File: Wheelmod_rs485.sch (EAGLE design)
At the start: 52 parts, among them IC1 SN75176BPSR, SW1 RST_SW, SW2 HWB_SW, U1 ATMEGA8U2AU, U2 SI8441IS1, U3 MC33887-HSOP, U4 NFET-SOIC8, U5 LDO, X1 MINI-USB, X2 MICROMATCH-4, X3 ENC, X4 MICROMATCH-4, X5 LOGIC_IN, Y1 SMDRESONATOR

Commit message: Testing
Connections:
- net A: no longer R5.1
- net B: no longer R5.2
- net RX: now also R5.2
- net TX: now also R5.1
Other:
- moved on the sheet: IC1, R5
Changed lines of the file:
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@@
 <?xml version="1.0" encoding="utf-8"?>
 <!DOCTYPE eagle SYSTEM "eagle.dtd">
-<eagle version="6.5.0">
+<eagle version="7.1.0">
 <drawing>
 <settings>
@@
 <instance part="C14" gate="G$1" x="170.18" y="119.38"/>
 <instance part="GND23" gate="1" x="170.18" y="109.22"/>
-<instance part="IC1" gate="G$1" x="-53.34" y="119.38"/>
-<instance part="R5" gate="G$1" x="-27.94" y="119.38" rot="R90"/>
-<instance part="P+5" gate="VCC" x="-38.1" y="134.62"/>
-<instance part="GND16" gate="1" x="-38.1" y="106.68"/>
+<instance part="IC1" gate="G$1" x="-38.1" y="121.92"/>
+<instance part="R5" gate="G$1" x="-66.04" y="121.92" rot="R90"/>
+<instance part="P+5" gate="VCC" x="-22.86" y="137.16"/>
+<instance part="GND16" gate="1" x="-22.86" y="109.22"/>
 <instance part="X2" gate="-1" x="-2.54" y="127"/>
 <instance part="X2" gate="-2" x="-2.54" y="124.46"/>
@@
 <pinref part="IC1" gate="G$1" pin="GND"/>
 <pinref part="GND16" gate="1" pin="GND"/>
-<wire x1="-40.64" y1="111.76" x2="-38.1" y2="111.76" width="0.1524" layer="91"/>
-<wire x1="-38.1" y1="111.76" x2="-38.1" y2="109.22" width="0.1524" layer="91"/>
+<wire x1="-25.4" y1="114.3" x2="-22.86" y2="114.3" width="0.1524" layer="91"/>
+<wire x1="-22.86" y1="114.3" x2="-22.86" y2="111.76" width="0.1524" layer="91"/>
 </segment>
 <segment>
@@
 <pinref part="IC1" gate="G$1" pin="VCC"/>
 <pinref part="P+5" gate="VCC" pin="VCC"/>
-<wire x1="-40.64" y1="127" x2="-38.1" y2="127" width="0.1524" layer="91"/>
-<wire x1="-38.1" y1="127" x2="-38.1" y2="132.08" width="0.1524" layer="91"/>
+<wire x1="-25.4" y1="129.54" x2="-22.86" y2="129.54" width="0.1524" layer="91"/>
+<wire x1="-22.86" y1="129.54" x2="-22.86" y2="134.62" width="0.1524" layer="91"/>
 </segment>
 <segment>
@@
 <segment>
 <pinref part="IC1" gate="G$1" pin="R"/>
-<wire x1="-66.04" y1="127" x2="-73.66" y2="127" width="0.1524" layer="91"/>
-<label x="-73.66" y="127" size="1.778" layer="95"/>
+<pinref part="R5" gate="G$1" pin="2"/>
+<wire x1="-50.8" y1="129.54" x2="-66.04" y2="129.54" width="0.1524" layer="91"/>
+<wire x1="-66.04" y1="129.54" x2="-66.04" y2="127" width="0.1524" layer="91"/>
+<wire x1="-66.04" y1="129.54" x2="-73.66" y2="129.54" width="0.1524" layer="91"/>
+<junction x="-66.04" y="129.54"/>
+<label x="-73.66" y="129.54" size="1.778" layer="95"/>
 </segment>
 <segment>
@@
 <segment>
 <pinref part="IC1" gate="G$1" pin="D"/>
-<wire x1="-66.04" y1="111.76" x2="-73.66" y2="111.76" width="0.1524" layer="91"/>
-<label x="-73.66" y="111.76" size="1.778" layer="95"/>
+<pinref part="R5" gate="G$1" pin="1"/>
+<wire x1="-50.8" y1="114.3" x2="-66.04" y2="114.3" width="0.1524" layer="91"/>
+<wire x1="-66.04" y1="114.3" x2="-66.04" y2="116.84" width="0.1524" layer="91"/>
+<wire x1="-66.04" y1="114.3" x2="-73.66" y2="114.3" width="0.1524" layer="91"/>
+<junction x="-66.04" y="114.3"/>
+<label x="-73.66" y="114.3" size="1.778" layer="95"/>
 </segment>
 <segment>
@@
 <pinref part="IC1" gate="G$1" pin="RE"/>
 <pinref part="IC1" gate="G$1" pin="DE"/>
-<wire x1="-66.04" y1="121.92" x2="-66.04" y2="116.84" width="0.1524" layer="91"/>
-<wire x1="-66.04" y1="116.84" x2="-73.66" y2="116.84" width="0.1524" layer="91"/>
-<junction x="-66.04" y="116.84"/>
-<label x="-73.66" y="116.84" size="1.778" layer="95"/>
+<wire x1="-50.8" y1="124.46" x2="-50.8" y2="119.38" width="0.1524" layer="91"/>
+<wire x1="-50.8" y1="119.38" x2="-58.42" y2="119.38" width="0.1524" layer="91"/>
+<junction x="-50.8" y="119.38"/>
+<label x="-58.42" y="119.38" size="1.778" layer="95"/>
 </segment>
 </net>
@@
 <segment>
 <pinref part="IC1" gate="G$1" pin="B"/>
-<wire x1="-40.64" y1="121.92" x2="-33.02" y2="121.92" width="0.1524" layer="91"/>
+<wire x1="-25.4" y1="124.46" x2="-17.78" y2="124.46" width="0.1524" layer="91"/>
 <label x="-25.4" y="124.46" size="1.778" layer="95"/>
-<wire x1="-33.02" y1="121.92" x2="-33.02" y2="124.46" width="0.1524" layer="91"/>
-<pinref part="R5" gate="G$1" pin="2"/>
-<wire x1="-33.02" y1="124.46" x2="-27.94" y2="124.46" width="0.1524" layer="91"/>
-<wire x1="-27.94" y1="124.46" x2="-22.86" y2="124.46" width="0.1524" layer="91"/>
-<junction x="-27.94" y="124.46"/>
 </segment>
 <segment>
@@
 <segment>
 <pinref part="IC1" gate="G$1" pin="A"/>
-<wire x1="-40.64" y1="116.84" x2="-33.02" y2="116.84" width="0.1524" layer="91"/>
-<label x="-25.4" y="114.3" size="1.778" layer="95"/>
-<wire x1="-33.02" y1="116.84" x2="-33.02" y2="114.3" width="0.1524" layer="91"/>
-<pinref part="R5" gate="G$1" pin="1"/>
-<wire x1="-33.02" y1="114.3" x2="-27.94" y2="114.3" width="0.1524" layer="91"/>
-<wire x1="-27.94" y1="114.3" x2="-22.86" y2="114.3" width="0.1524" layer="91"/>
-<junction x="-27.94" y="114.3"/>
-</segment>
-<segment>
+<wire x1="-25.4" y1="119.38" x2="-17.78" y2="119.38" width="0.1524" layer="91"/>
+<label x="-25.4" y="119.38" size="1.778" layer="95"/>
+</segment>
+<segment>

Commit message: Testing2
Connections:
- net A: now also R5.1
- net B: now also R5.2
- net RX: no longer R5.2
- net TX: no longer R5.1
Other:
- moved on the sheet: IC1, R5
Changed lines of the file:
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@@
 <?xml version="1.0" encoding="utf-8"?>
 <!DOCTYPE eagle SYSTEM "eagle.dtd">
-<eagle version="7.1.0">
+<eagle version="6.5.0">
 <drawing>
 <settings>
@@
 <instance part="C14" gate="G$1" x="170.18" y="119.38"/>
 <instance part="GND23" gate="1" x="170.18" y="109.22"/>
-<instance part="IC1" gate="G$1" x="-38.1" y="121.92"/>
-<instance part="R5" gate="G$1" x="-66.04" y="121.92" rot="R90"/>
-<instance part="P+5" gate="VCC" x="-22.86" y="137.16"/>
-<instance part="GND16" gate="1" x="-22.86" y="109.22"/>
+<instance part="IC1" gate="G$1" x="-53.34" y="119.38"/>
+<instance part="R5" gate="G$1" x="-27.94" y="119.38" rot="R90"/>
+<instance part="P+5" gate="VCC" x="-38.1" y="134.62"/>
+<instance part="GND16" gate="1" x="-38.1" y="106.68"/>
 <instance part="X2" gate="-1" x="-2.54" y="127"/>
 <instance part="X2" gate="-2" x="-2.54" y="124.46"/>
@@
 <pinref part="IC1" gate="G$1" pin="GND"/>
 <pinref part="GND16" gate="1" pin="GND"/>
-<wire x1="-25.4" y1="114.3" x2="-22.86" y2="114.3" width="0.1524" layer="91"/>
-<wire x1="-22.86" y1="114.3" x2="-22.86" y2="111.76" width="0.1524" layer="91"/>
+<wire x1="-40.64" y1="111.76" x2="-38.1" y2="111.76" width="0.1524" layer="91"/>
+<wire x1="-38.1" y1="111.76" x2="-38.1" y2="109.22" width="0.1524" layer="91"/>
 </segment>
 <segment>
@@
 <pinref part="IC1" gate="G$1" pin="VCC"/>
 <pinref part="P+5" gate="VCC" pin="VCC"/>
-<wire x1="-25.4" y1="129.54" x2="-22.86" y2="129.54" width="0.1524" layer="91"/>
-<wire x1="-22.86" y1="129.54" x2="-22.86" y2="134.62" width="0.1524" layer="91"/>
+<wire x1="-40.64" y1="127" x2="-38.1" y2="127" width="0.1524" layer="91"/>
+<wire x1="-38.1" y1="127" x2="-38.1" y2="132.08" width="0.1524" layer="91"/>
 </segment>
 <segment>
@@
 <segment>
 <pinref part="IC1" gate="G$1" pin="R"/>
-<pinref part="R5" gate="G$1" pin="2"/>
-<wire x1="-50.8" y1="129.54" x2="-66.04" y2="129.54" width="0.1524" layer="91"/>
-<wire x1="-66.04" y1="129.54" x2="-66.04" y2="127" width="0.1524" layer="91"/>
-<wire x1="-66.04" y1="129.54" x2="-73.66" y2="129.54" width="0.1524" layer="91"/>
-<junction x="-66.04" y="129.54"/>
-<label x="-73.66" y="129.54" size="1.778" layer="95"/>
+<wire x1="-66.04" y1="127" x2="-73.66" y2="127" width="0.1524" layer="91"/>
+<label x="-73.66" y="127" size="1.778" layer="95"/>
 </segment>
 <segment>
@@
 <segment>
 <pinref part="IC1" gate="G$1" pin="D"/>
-<pinref part="R5" gate="G$1" pin="1"/>
-<wire x1="-50.8" y1="114.3" x2="-66.04" y2="114.3" width="0.1524" layer="91"/>
-<wire x1="-66.04" y1="114.3" x2="-66.04" y2="116.84" width="0.1524" layer="91"/>
-<wire x1="-66.04" y1="114.3" x2="-73.66" y2="114.3" width="0.1524" layer="91"/>
-<junction x="-66.04" y="114.3"/>
-<label x="-73.66" y="114.3" size="1.778" layer="95"/>
+<wire x1="-66.04" y1="111.76" x2="-73.66" y2="111.76" width="0.1524" layer="91"/>
+<label x="-73.66" y="111.76" size="1.778" layer="95"/>
 </segment>
 <segment>
@@
 <pinref part="IC1" gate="G$1" pin="RE"/>
 <pinref part="IC1" gate="G$1" pin="DE"/>
-<wire x1="-50.8" y1="124.46" x2="-50.8" y2="119.38" width="0.1524" layer="91"/>
-<wire x1="-50.8" y1="119.38" x2="-58.42" y2="119.38" width="0.1524" layer="91"/>
-<junction x="-50.8" y="119.38"/>
-<label x="-58.42" y="119.38" size="1.778" layer="95"/>
+<wire x1="-66.04" y1="121.92" x2="-66.04" y2="116.84" width="0.1524" layer="91"/>
+<wire x1="-66.04" y1="116.84" x2="-73.66" y2="116.84" width="0.1524" layer="91"/>
+<junction x="-66.04" y="116.84"/>
+<label x="-73.66" y="116.84" size="1.778" layer="95"/>
 </segment>
 </net>
@@
 <segment>
 <pinref part="IC1" gate="G$1" pin="B"/>
-<wire x1="-25.4" y1="124.46" x2="-17.78" y2="124.46" width="0.1524" layer="91"/>
+<wire x1="-40.64" y1="121.92" x2="-33.02" y2="121.92" width="0.1524" layer="91"/>
 <label x="-25.4" y="124.46" size="1.778" layer="95"/>
+<wire x1="-33.02" y1="121.92" x2="-33.02" y2="124.46" width="0.1524" layer="91"/>
+<pinref part="R5" gate="G$1" pin="2"/>
+<wire x1="-33.02" y1="124.46" x2="-27.94" y2="124.46" width="0.1524" layer="91"/>
+<wire x1="-27.94" y1="124.46" x2="-22.86" y2="124.46" width="0.1524" layer="91"/>
+<junction x="-27.94" y="124.46"/>
 </segment>
 <segment>
@@
 <segment>
 <pinref part="IC1" gate="G$1" pin="A"/>
-<wire x1="-25.4" y1="119.38" x2="-17.78" y2="119.38" width="0.1524" layer="91"/>
-<label x="-25.4" y="119.38" size="1.778" layer="95"/>
-</segment>
-<segment>
+<wire x1="-40.64" y1="116.84" x2="-33.02" y2="116.84" width="0.1524" layer="91"/>
+<label x="-25.4" y="114.3" size="1.778" layer="95"/>
+<wire x1="-33.02" y1="116.84" x2="-33.02" y2="114.3" width="0.1524" layer="91"/>
+<pinref part="R5" gate="G$1" pin="1"/>
+<wire x1="-33.02" y1="114.3" x2="-27.94" y2="114.3" width="0.1524" layer="91"/>
+<wire x1="-27.94" y1="114.3" x2="-22.86" y2="114.3" width="0.1524" layer="91"/>
+<junction x="-27.94" y="114.3"/>
+</segment>
+<segment>

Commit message: Some changes to board and gerber files for production.
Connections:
- removed net N$22: F1.1, X2-1.S
- new net N$32: F1.1, X2-2.S
- net B: now also X2-4.S; no longer X2-2.S
- net GND: now also X2-1.S; no longer X2-4.S
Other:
- note added: "wheelmod v0.7"
- note removed: "wheelmod v0.6"
- moved on the sheet: C15, F1
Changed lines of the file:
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@@
 <?xml version="1.0" encoding="utf-8"?>
 <!DOCTYPE eagle SYSTEM "eagle.dtd">
-<eagle version="6.5.0">
+<eagle version="7.0.0">
 <drawing>
 <settings>
@@
 <sheet>
 <plain>
-<text x="208.28" y="7.62" size="5.08" layer="94">wheelmod v0.6</text>
+<text x="208.28" y="7.62" size="5.08" layer="94">wheelmod v0.7</text>
 </plain>
 <instances>
@@
 <instance part="X2" gate="-3" x="-2.54" y="121.92"/>
 <instance part="X2" gate="-4" x="-2.54" y="119.38"/>
-<instance part="GND24" gate="1" x="2.54" y="111.76" rot="MR0"/>
-<instance part="F1" gate="G$1" x="12.7" y="127"/>
-<instance part="P+11" gate="VCC" x="20.32" y="137.16"/>
-<instance part="C15" gate="G$1" x="20.32" y="121.92"/>
-<instance part="GND25" gate="1" x="20.32" y="114.3"/>
+<instance part="GND24" gate="1" x="33.02" y="111.76" rot="MR0"/>
+<instance part="F1" gate="G$1" x="12.7" y="124.46"/>
+<instance part="P+11" gate="VCC" x="20.32" y="134.62"/>
+<instance part="C15" gate="G$1" x="20.32" y="119.38"/>
+<instance part="GND25" gate="1" x="20.32" y="111.76"/>
 <instance part="X4" gate="-1" x="66.04" y="76.2" rot="R180"/>
 <instance part="X4" gate="-2" x="66.04" y="78.74" rot="R180"/>
@@
 </segment>
 <segment>
-<pinref part="GND24" gate="1" pin="GND"/>
-<pinref part="X2" gate="-4" pin="S"/>
-<wire x1="2.54" y1="114.3" x2="2.54" y2="119.38" width="0.1524" layer="91"/>
-</segment>
-<segment>
 <pinref part="C15" gate="G$1" pin="2"/>
 <pinref part="GND25" gate="1" pin="GND"/>
+</segment>
+<segment>
+<pinref part="X2" gate="-1" pin="S"/>
+<wire x1="2.54" y1="127" x2="33.02" y2="127" width="0.1524" layer="91"/>
+<pinref part="GND24" gate="1" pin="GND"/>
+<wire x1="33.02" y1="127" x2="33.02" y2="114.3" width="0.1524" layer="91"/>
 </segment>
 </net>
@@
 <pinref part="P+9" gate="VCC" pin="VCC"/>
 <pinref part="C1" gate="G$1" pin="1"/>
-<label x="22.86" y="127" size="1.778" layer="95"/>
+<label x="22.86" y="124.46" size="1.778" layer="95"/>
 </segment>
 <segment>
@@
 <segment>
 <pinref part="P+11" gate="VCC" pin="VCC"/>
-<wire x1="20.32" y1="127" x2="20.32" y2="134.62" width="0.1524" layer="91"/>
+<wire x1="20.32" y1="124.46" x2="20.32" y2="132.08" width="0.1524" layer="91"/>
 <pinref part="F1" gate="G$1" pin="2"/>
-<junction x="20.32" y="127"/>
+<junction x="20.32" y="124.46"/>
 <pinref part="C15" gate="G$1" pin="1"/>
-<wire x1="20.32" y1="124.46" x2="20.32" y2="127" width="0.1524" layer="91"/>
-<wire x1="20.32" y1="127" x2="30.48" y2="127" width="0.1524" layer="91"/>
+<wire x1="20.32" y1="121.92" x2="20.32" y2="124.46" width="0.1524" layer="91"/>
+<wire x1="20.32" y1="124.46" x2="30.48" y2="124.46" width="0.1524" layer="91"/>
 </segment>
 </net>
@@
 </segment>
 </net>
-<net name="N$22" class="0">
-<segment>
-<pinref part="X2" gate="-1" pin="S"/>
-<pinref part="F1" gate="G$1" pin="1"/>
-<wire x1="2.54" y1="127" x2="7.62" y2="127" width="0.1524" layer="91"/>
-</segment>
-</net>
 <net name="B" class="0">
 <segment>
@@
 </segment>
 <segment>
-<pinref part="X2" gate="-2" pin="S"/>
-<wire x1="2.54" y1="124.46" x2="7.62" y2="124.46" width="0.1524" layer="91"/>
-<wire x1="7.62" y1="124.46" x2="7.62" y2="116.84" width="0.1524" layer="91"/>
-<wire x1="7.62" y1="116.84" x2="15.24" y2="116.84" width="0.1524" layer="91"/>
-<label x="10.16" y="116.84" size="1.778" layer="95"/>
+<pinref part="X2" gate="-4" pin="S"/>
+<wire x1="2.54" y1="119.38" x2="7.62" y2="119.38" width="0.1524" layer="91"/>
+<label x="2.54" y="119.38" size="1.778" layer="95"/>
 </segment>
 </net>
@@
 <segment>
 <pinref part="X2" gate="-3" pin="S"/>
-<wire x1="2.54" y1="121.92" x2="5.08" y2="121.92" width="0.1524" layer="91"/>
-<wire x1="5.08" y1="121.92" x2="5.08" y2="114.3" width="0.1524" layer="91"/>
-<wire x1="5.08" y1="114.3" x2="15.24" y2="114.3" width="0.1524" layer="91"/>
-<label x="10.16" y="114.3" size="1.778" layer="95"/>
+<wire x1="2.54" y1="121.92" x2="7.62" y2="121.92" width="0.1524" layer="91"/>
+<label x="2.54" y="121.92" size="1.778" layer="95"/>
 </segment>
 </net>
@@
 </segment>
 </net>
+<net name="N$32" class="0">
+<segment>
+<pinref part="X2" gate="-2" pin="S"/>
+<pinref part="F1" gate="G$1" pin="1"/>
+<wire x1="2.54" y1="124.46" x2="7.62" y2="124.46" width="0.1524" layer="91"/>
+</segment>
+</net>

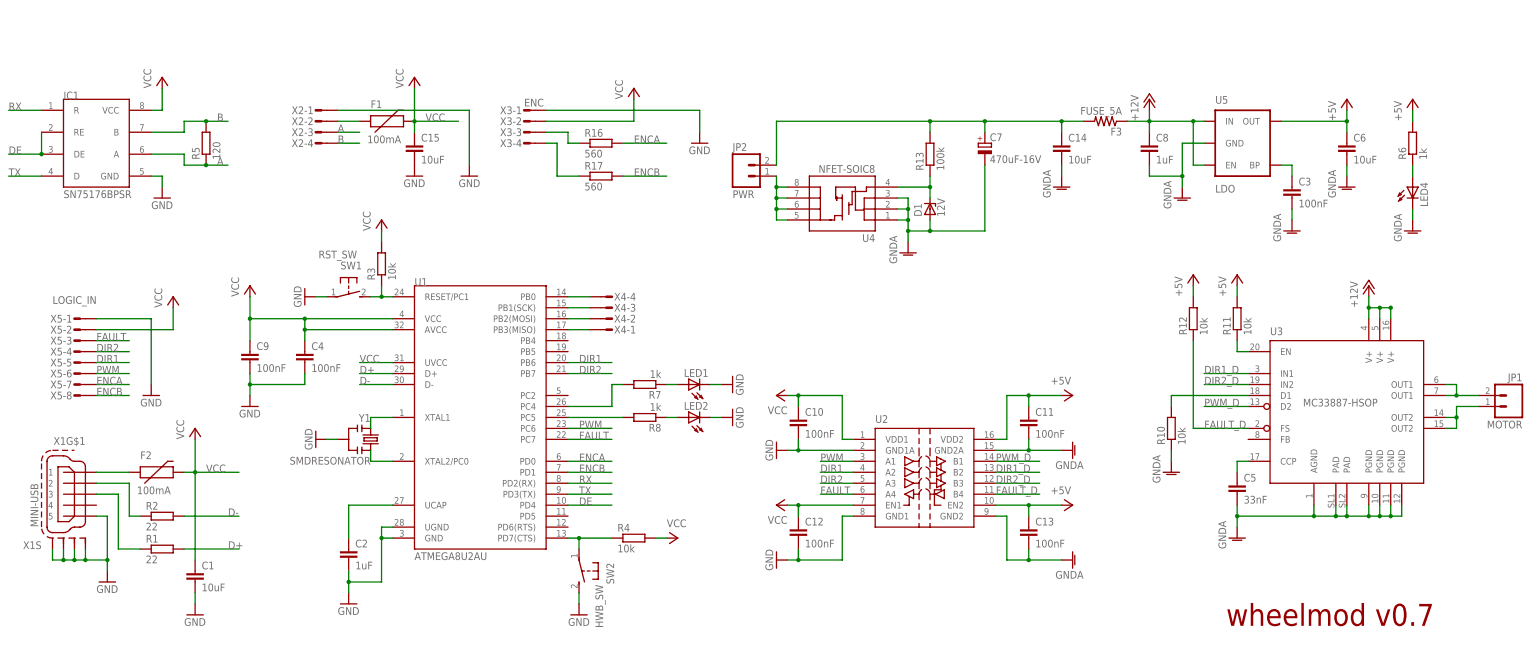
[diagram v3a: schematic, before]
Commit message: Full duplex tugi kommunikatsioonimoodulit
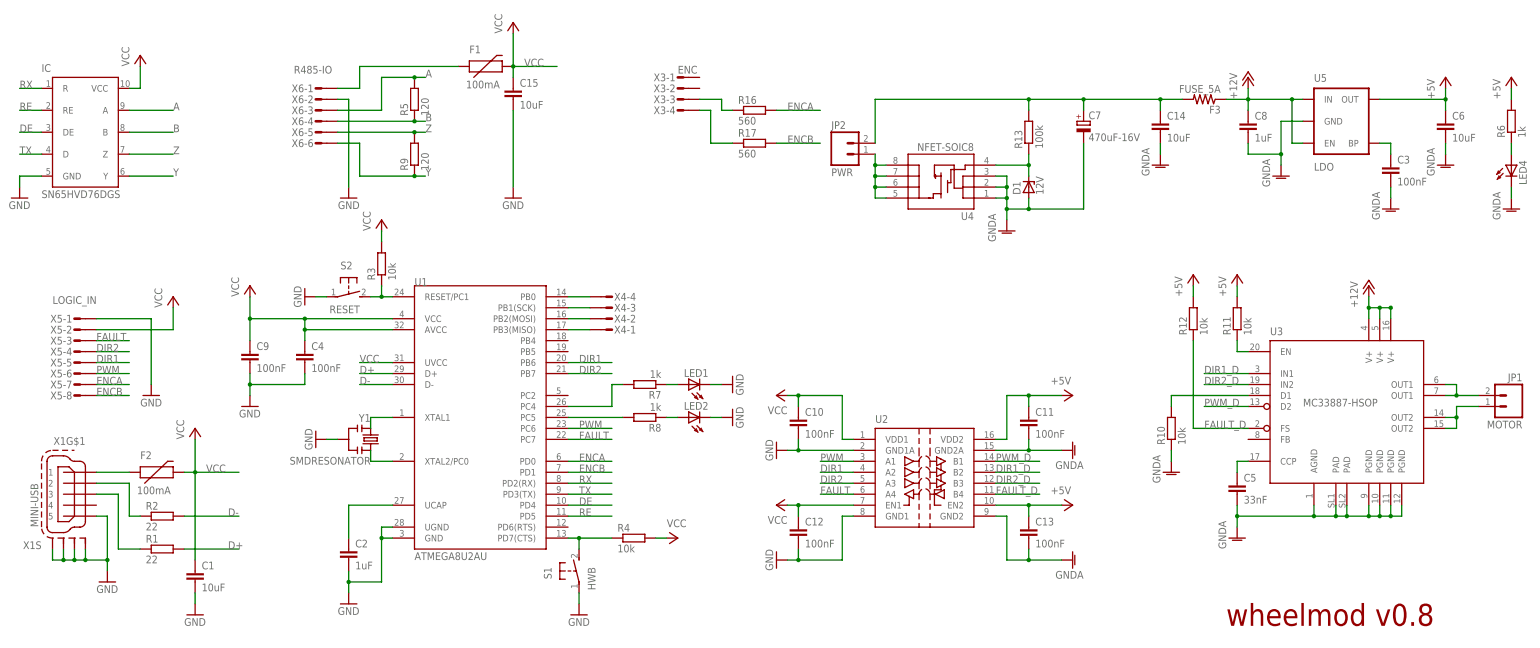
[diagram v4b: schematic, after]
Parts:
- removed IC1: SN75176BPSR, rs485DRIVER:SN75176BPSR
- removed SW1: RST_SW, Erik:SMD-TACT-3.9X2.9
- removed SW2: HWB_SW, Erik:SMD-TACT-3.9X2.9
- removed X2: MICROMATCH-4, con-amp-micromatch:MICROMATCH-4
- added R9: 120, rcl:R-EU_R0603
- added S1: HWB, kommunikatsioonimoodul:ADTSM3
- added S2: RESET, kommunikatsioonimoodul:ADTSM3
- added U$1: SN65HVF76DGS, rs485:SN65HVF76DGS
- added X6: R485-IO, con-amp-micromatch:MICROMATCH-6
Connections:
- removed net N$32: F1.1, X2-2.S
- new net N$33: F1.1, X6-1.S
- new net RE: U$1.RE, U1.PD5
- new net Y: R9.1, U$1.Y, X6-6.S
- new net Z: R9.2, U$1.Z, X6-5.S
- net A: now also R5.2, U$1.A, X6-3.S; no longer IC1.A, R5.1, X2-3.S
- net B: now also R5.1, U$1.B, X6-4.S; no longer IC1.B, R5.2, X2-4.S
- net DE: now also U$1.DE; no longer IC1.DE, IC1.RE
- net GND: now also S1.1, S2.1, U$1.GND, X6-2.S; no longer IC1.GND, SW1.1, SW2.2, X2-1.S, X3-1.S
- net N$10: now also S2.2; no longer SW1.2
- net N$2: now also S1.2; no longer SW2.1
- net RX: now also U$1.R; no longer IC1.R
- net TX: now also U$1.D; no longer IC1.D
- net VCC: now also U$1.VCC; no longer IC1.VCC, X3-2.S
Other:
- note added: "wheelmod v0.8"
- note removed: "wheelmod v0.7"
- moved on the sheet: C14, C15, C3, C6, C7, C8, D1, F1, F3, JP2, LED4, R13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
